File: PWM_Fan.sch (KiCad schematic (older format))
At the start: 6 parts, among them Q1 Q_PMOS_GDS

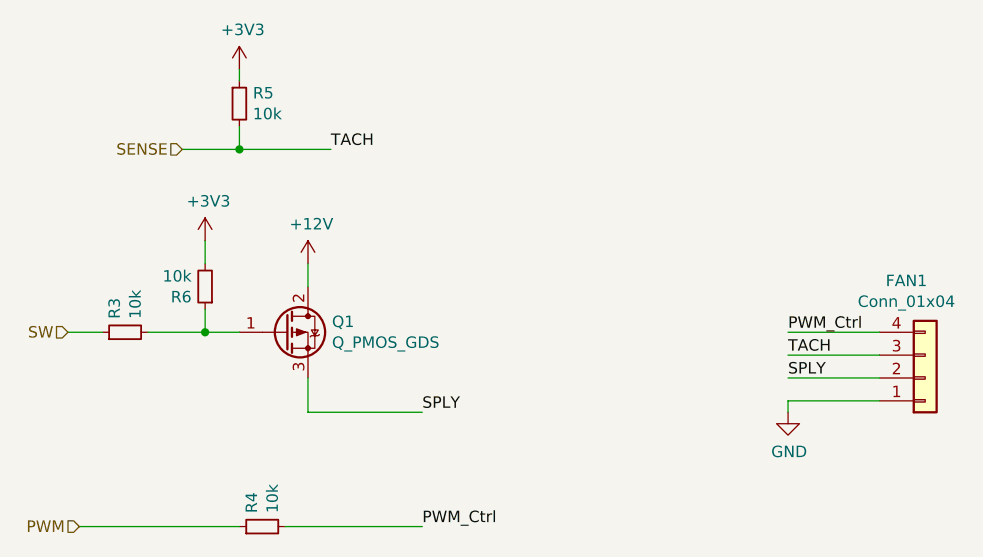
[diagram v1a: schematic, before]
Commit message: First iteration with new ES32 - but not S2
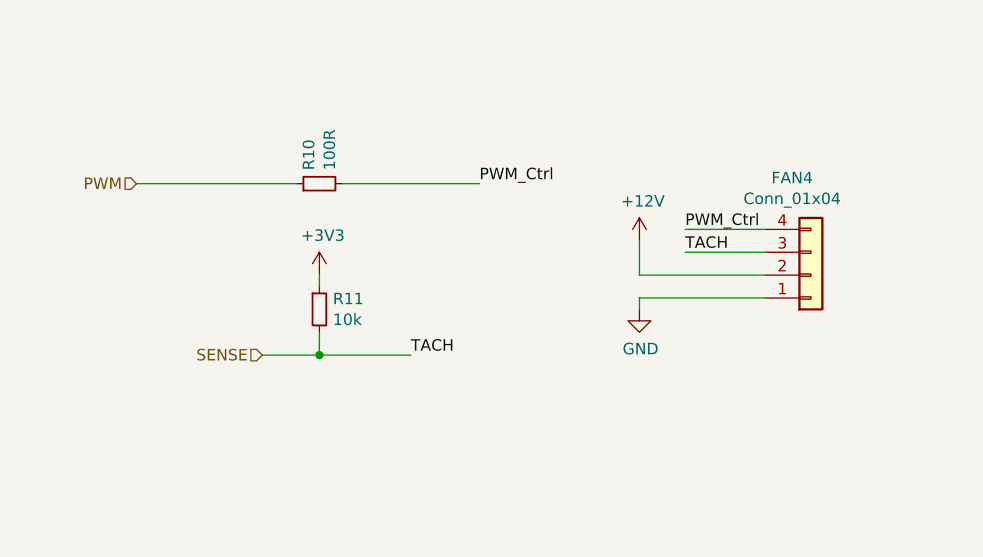
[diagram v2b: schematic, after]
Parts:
- removed Q1: Q_PMOS_GDS, Package_TO_SOT_SMD:SOT-23, symbol Device:Q_PMOS_GDS
- removed R3, R6: 10k, Resistor_SMD:R_0805_2012Metric, symbol Device:R_Small
- R4: value 10k -> 100R; LCSC (none) -> C17408
- R5: LCSC (none) -> C17414
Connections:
- net SPLY is gone; now on net +12V: FAN1.2 (Pin_2)
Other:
- moved on the sheet: FAN4, R10, R11

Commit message: Version open for review
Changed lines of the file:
@@
 AR Path="/6195792B/618B3143" Ref="R8"  Part="1"
 AR Path="/61958B6F/618B3143" Ref="R10"  Part="1"
-F 0 "R10" H 4409 2696 50  0000 L CNN
+F 0 "R4" H 4409 2696 50  0000 L CNN
 F 1 "100R" H 4409 2605 50  0000 L CNN
 F 2 "Resistor_SMD:R_0805_2012Metric" H 4350 2650 50  0001 C CNN
@@
 AR Path="/6195792B/618A77D7" Ref="R9"  Part="1"
 AR Path="/61958B6F/618A77D7" Ref="R11"  Part="1"
-F 0 "R11" H 4409 3246 50  0000 L CNN
+F 0 "R5" H 4409 3246 50  0000 L CNN
 F 1 "10k" H 4409 3155 50  0000 L CNN
 F 2 "Resistor_SMD:R_0805_2012Metric" H 4350 3200 50  0001 C CNN
@@
 AR Path="/6195792B/618A77D4" Ref="FAN3"  Part="1"
 AR Path="/61958B6F/618A77D4" Ref="FAN4"  Part="1"
-F 0 "FAN4" H 6418 2625 50  0000 C CNN
+F 0 "FAN1" H 6418 2625 50  0000 C CNN
 F 1 "Conn_01x04" H 6418 2716 50  0000 C CNN
 F 2 "Connector:FanPinHeader_1x04_P2.54mm_Vertical" H 6500 3050 50  0001 C CNN
